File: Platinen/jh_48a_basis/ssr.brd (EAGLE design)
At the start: 27.6 x 11.4 mm, 6 parts, among them T1 BT136

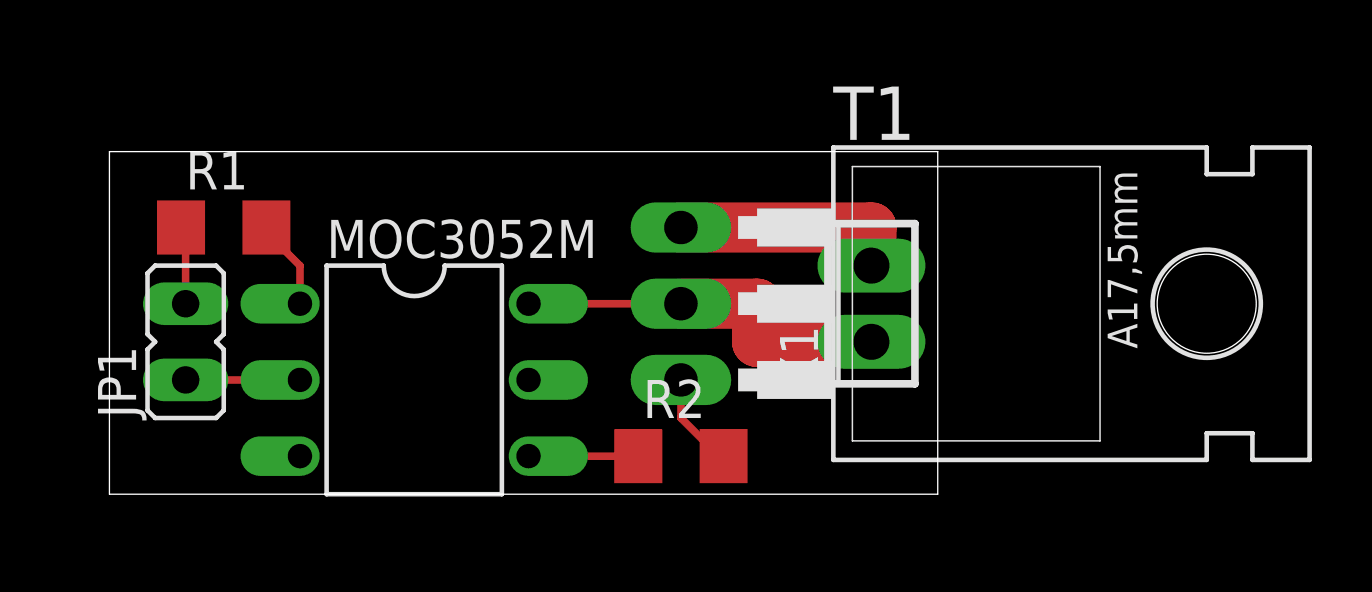
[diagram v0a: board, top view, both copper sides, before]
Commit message: layout: update ssr board
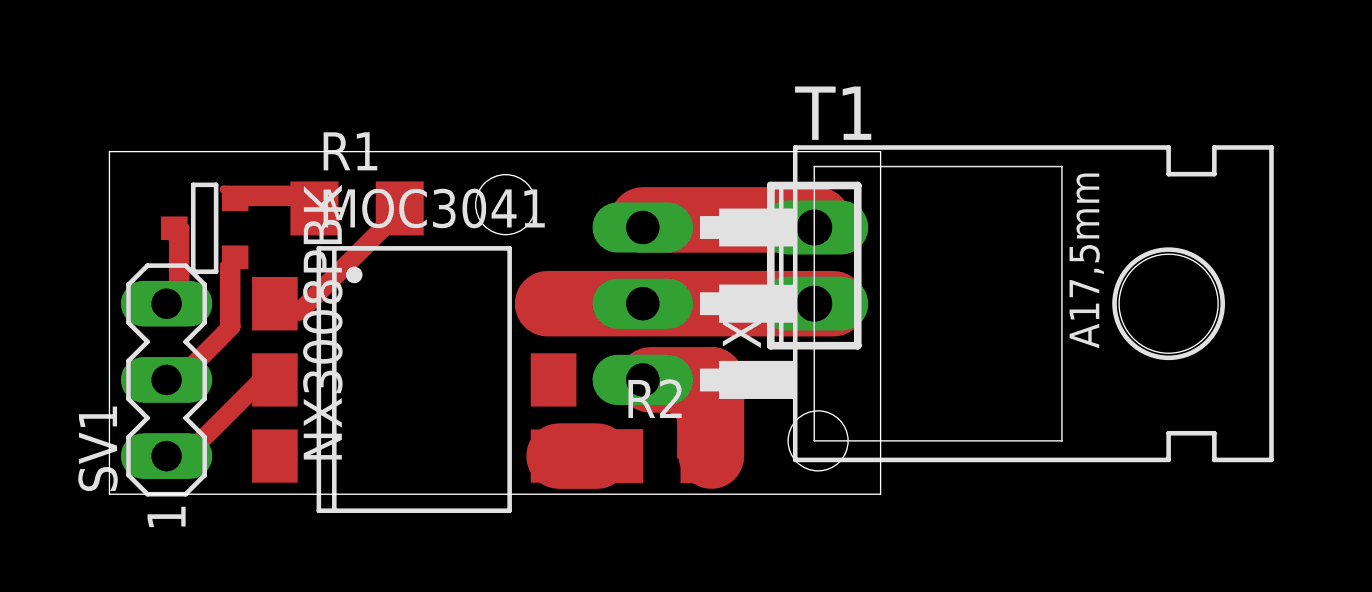
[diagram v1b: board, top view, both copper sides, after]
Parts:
- removed JP1: (no value), jumper:JP1
- removed MOC3052M: MOC3031M, optocoupler:DIL06
- added MOC3041: MOC3041S, optocoupler:DIL6-SMD
- added NX3008PBK: (no value), zetex:SOT-23
- added SV1: (no value), con-lstb:MA03-1
- moved R1 4.49 mm to (8.26, 9.53)
- moved X1 2.29 mm to (23.5, 7.62)
- moved T1 1.27 mm to (24.1, 6.35)
- moved R2 0.64 mm to (18.4, 1.27)
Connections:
- new net N$7: NX3008PBK.3, SV1.2
- new net N$8: NX3008PBK.1, SV1.3
- net GND: now also MOC3041.2, SV1.1; no longer JP1.1, MOC3052M.2
- net N$1: now also MOC3041.1; no longer MOC3052M.1
- net N$2: now also NX3008PBK.2; no longer JP1.2
- net N$3: now also MOC3041.4; no longer MOC3052M.4
- net N$5: now also MOC3041.6; no longer MOC3052M.6
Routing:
- net N$7: track 0.00 -> 10.5 mm
- net N$9: track 0.00 -> 9.52 mm
- net N$8: track 0.00 -> 6.10 mm
- net N$10: track 0.00 -> 5.84 mm
- net N$13: track 0.00 -> 4.92 mm
- net GND: track 3.81 -> 8.61 mm
- net N$11: track 0.00 -> 4.57 mm
- net N$5: track 12.7 -> 8.69 mm
- net N$1: track 3.22 -> 5.87 mm
- net N$12: track 0.00 -> 2.29 mm
- net N$6: track 7.62 -> 5.71 mm
- net N$3: track 3.81 -> 2.19 mm
- net N$2: track 2.69 -> 3.84 mm
- net N$4: track 3.22 -> 3.85 mm
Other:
- board size 27.6 x 11.4 mm -> 25.7 x 11.4 mm
